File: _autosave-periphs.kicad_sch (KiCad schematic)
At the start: 1 part, among them U501 STM32L552ZET6Q

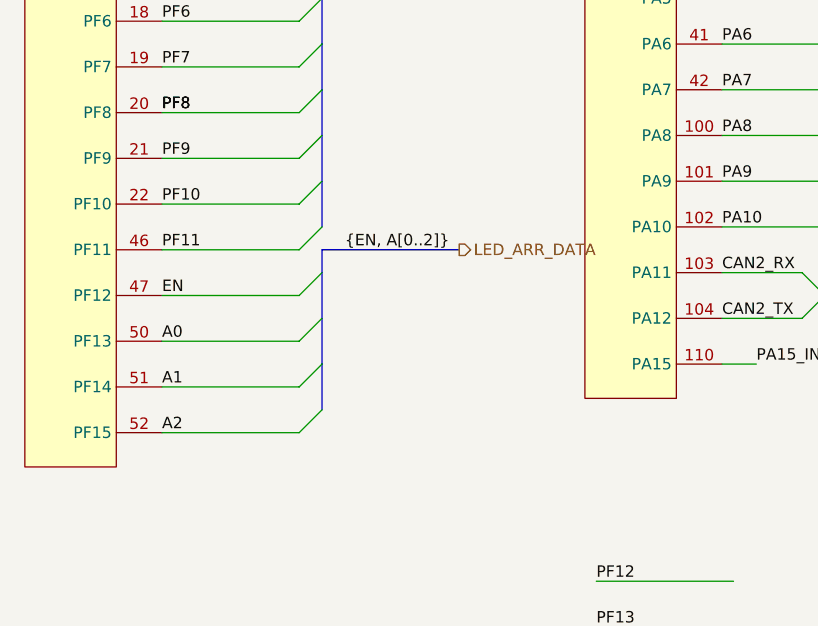
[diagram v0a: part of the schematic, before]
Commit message: slimed out gpio conns, changed to 6layer
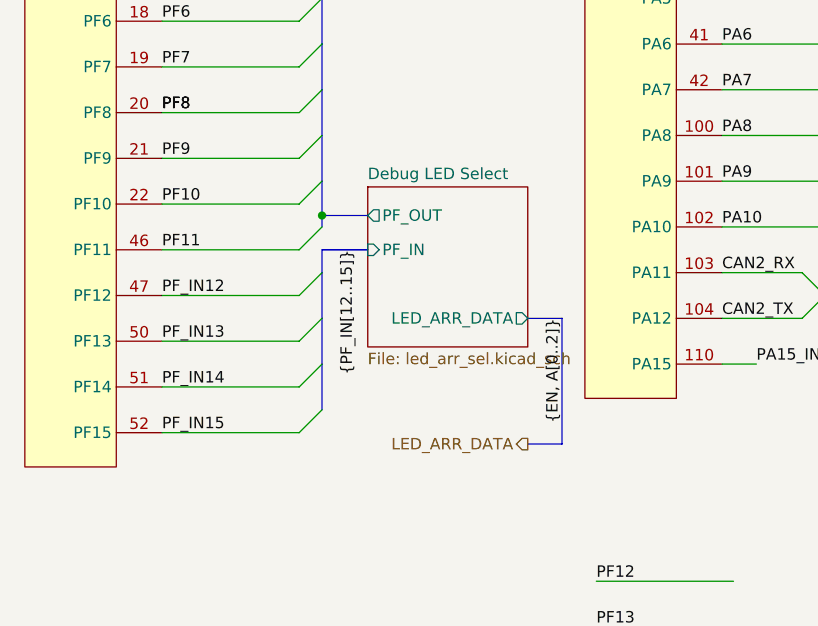
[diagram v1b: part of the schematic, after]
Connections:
- net A0 renamed PF_IN13
- net A1 renamed PF_IN14
- net A2 renamed PF_IN15
- net EN renamed PF_IN12
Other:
- added sheet Debug LED Select (led_arr_sel.kicad_sch)
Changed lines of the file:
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@@
 	(generator_version "9.0")
 	(paper "A4")
+	(junction
+		(at 107.95 167.64)
+		(diameter 0)
+		(color 0 0 0 0)
+	)
 	(bus_entry
 		(at 123.19 57.15)
@@
 	(bus
 		(pts
+			(xy 130.81 179.07) (xy 134.62 179.07)
+		)
+		(stroke
+			(width 0)
+			(type default)
+		)
+	)
+	(bus
+		(pts
 			(xy 191.77 86.36) (xy 191.77 101.6)
 		)
@@
 	(bus
 		(pts
-			(xy 107.95 171.45) (xy 123.19 171.45)
+			(xy 107.95 171.45) (xy 113.03 171.45)
 		)
 		(stroke
@@
 		)
 	)
+	(bus
+		(pts
+			(xy 134.62 179.07) (xy 134.62 193.04)
+		)
+		(stroke
+			(width 0)
+			(type default)
+		)
+	)
 	(wire
 		(pts
@@
 		)
 	)
+	(bus
+		(pts
+			(xy 107.95 167.64) (xy 113.03 167.64)
+		)
+		(stroke
+			(width 0)
+			(type default)
+		)
+	)
 	(wire
 		(pts
@@
 	(bus
 		(pts
+			(xy 107.95 163.83) (xy 107.95 167.64)
+		)
+		(stroke
+			(width 0)
+			(type default)
+		)
+	)
+	(bus
+		(pts
 			(xy 48.26 153.67) (xy 48.26 158.75)
 		)
@@
 	(bus
 		(pts
-			(xy 107.95 163.83) (xy 107.95 168.91)
+			(xy 107.95 167.64) (xy 107.95 168.91)
 		)
 		(stroke
@@
 		)
 	)
+	(bus
+		(pts
+			(xy 130.81 193.04) (xy 134.62 193.04)
+		)
+		(stroke
+			(width 0)
+			(type default)
+		)
+	)
 	(wire
 		(pts
@@
 		)
 	)
-	(label "A1"
-		(at 90.17 186.69 0)
-		(effects
-			(font
-				(size 1.27 1.27)
-			)
-			(justify left bottom)
-		)
-	)
 	(label "PG3"
 		(at 29.21 46.99 0)
@@
 		)
 	)
+	(label "{PF_IN[12..15]}"
+		(at 111.76 171.45 270)
+		(effects
+			(font
+				(size 1.27 1.27)
+			)
+			(justify right bottom)
+		)
+	)
 	(label "PF5"
 		(at 90.17 140.97 0)
@@
 	)
 	(label "{EN, A[0..2]}"
-		(at 110.49 171.45 0)
+		(at 134.62 179.07 270)
 		(effects
 			(font
 				(size 1.27 1.27)
 			)
-			(justify left bottom)
+			(justify right bottom)
 		)
 	)
@@
 		)
 	)
+	(label "PF_IN15"
+		(at 90.17 191.77 0)
+		(effects
+			(font
+				(size 1.27 1.27)
+			)
+			(justify left bottom)
+		)
+	)
 	(label "PE4"
 		(at 30.48 135.89 0)
@@
 		)
 	)
-	(label "A0"
-		(at 90.17 181.61 0)
-		(effects
-			(font
-				(size 1.27 1.27)
-			)
-			(justify left bottom)
-		)
-	)
 	(label "PB2"
 		(at 107.95 36.83 0)
@@
 		)
 	)
+	(label "PF_IN13"
+		(at 90.17 181.61 0)
+		(effects
+			(font
+				(size 1.27 1.27)
+			)
+			(justify left bottom)
+		)
+	)
 	(label "PC3"
 		(at 180.34 48.26 0)
@@
 		)
 	)
+	(label "PF_IN12"
+		(at 90.17 176.53 0)
+		(effects
+			(font
+				(size 1.27 1.27)
+			)
+			(justify left bottom)
+		)
+	)
 	(label "PF8"
 		(at 90.17 156.21 0)
@@
 		)
 	)
-	(label "EN"
-		(at 90.17 176.53 0)
+	(label "PF_IN14"
+		(at 90.17 186.69 0)
 		(effects
 			(font
@@
 		)
 	)
-	(label "A2"
-		(at 90.17 191.77 0)
-		(effects
-			(font
-				(size 1.27 1.27)
-			)
-			(justify left bottom)
-		)
-	)
 	(label "PA3"
 		(at 152.4 133.35 0)
@@
 		)
 	)
+	(hierarchical_label "LED_ARR_DATA"
+		(shape output)
+		(at 130.81 193.04 180)
+		(effects
+			(font
+				(size 1.27 1.27)
+			)
+			(justify right)
+		)
+	)
 	(hierarchical_label "PGout"
 		(shape bidirectional)
@@
 		)
 	)
-	(hierarchical_label "LED_ARR_DATA"
-		(shape output)
-		(at 123.19 171.45 0)
-		(effects
-			(font
-				(size 1.27 1.27)
-			)
-			(justify left)
-		)
-	)
 	(hierarchical_label "PCout"
 		(shape bidirectional)
@@
 				)
 			)
+		)
+	)
+	(sheet
+		(at 113.03 164.465)
+		(size 17.78 17.78)
+		(exclude_from_sim no)
+		(in_bom yes)
+		(on_board yes)
+		(dnp no)
+		(fields_autoplaced yes)
+		(stroke
+			(width 0.1524)
+			(type solid)
+		)
+		(fill
+			(color 255 255 194 1.0000)
+		)
+		(property "Sheetname" "Debug LED Select"
+			(at 113.03 163.7534 0)
+			(effects
+				(font
+					(size 1.27 1.27)
+				)
+				(justify left bottom)
+			)
+		)
+		(property "Sheetfile" "led_arr_sel.kicad_sch"
+			(at 113.03 182.8296 0)
+			(effects
+				(font
+					(size 1.27 1.27)
+				)
+				(justify left top)
+			)
+		)
+		(pin "PF_IN" input
+			(at 113.03 171.45 180)
+			(effects
+				(font
+					(size 1.27 1.27)
+				)
+				(justify left)
+			)
+		)
+		(pin "PF_OUT" output
+			(at 113.03 167.64 180)
+			(effects
+				(font
+					(size 1.27 1.27)
+				)
+				(justify left)
+			)
+		)
+		(pin "LED_ARR_DATA" output
+			(at 130.81 179.07 0)
+			(effects
+				(font
+					(size 1.27 1.27)
+				)
+				(justify right)
+			)
+		)
+		(instances
+			(project "DU UC V1 - Minnow"
+				(path "/0aeff2df-21bc-4c76-95d6-83ff8577a8db/479988e2-73e3-4e6d-8b3c-5b8d2874850c/a5605b2d-f7ac-45f3-aba3-2f27c488895b"
+					(page "17")
+				)
+			)
